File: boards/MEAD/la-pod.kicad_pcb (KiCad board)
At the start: 4 copper layers, 75 x 97.5 mm, 199 parts, among them J1 CONN_SFF8087, J2 PINHEADER_1x5, J3 LSHM-120-02.5-L-DV-A-N-K-TR, J4 AMG240160P-G-W6WFDW, J5 PINHEADER_1x2, U1 LMH7322, U14 TPS62173, U15 LM27761, U2 LMH7322, U3 LMH7322, U4 LMH7322, U5 STM32F031-QFN28, U6 DAC60508ZRTET, U7 TPS62170, U8 LP5907SNX-3.3/NOPB, U9 TPS62170

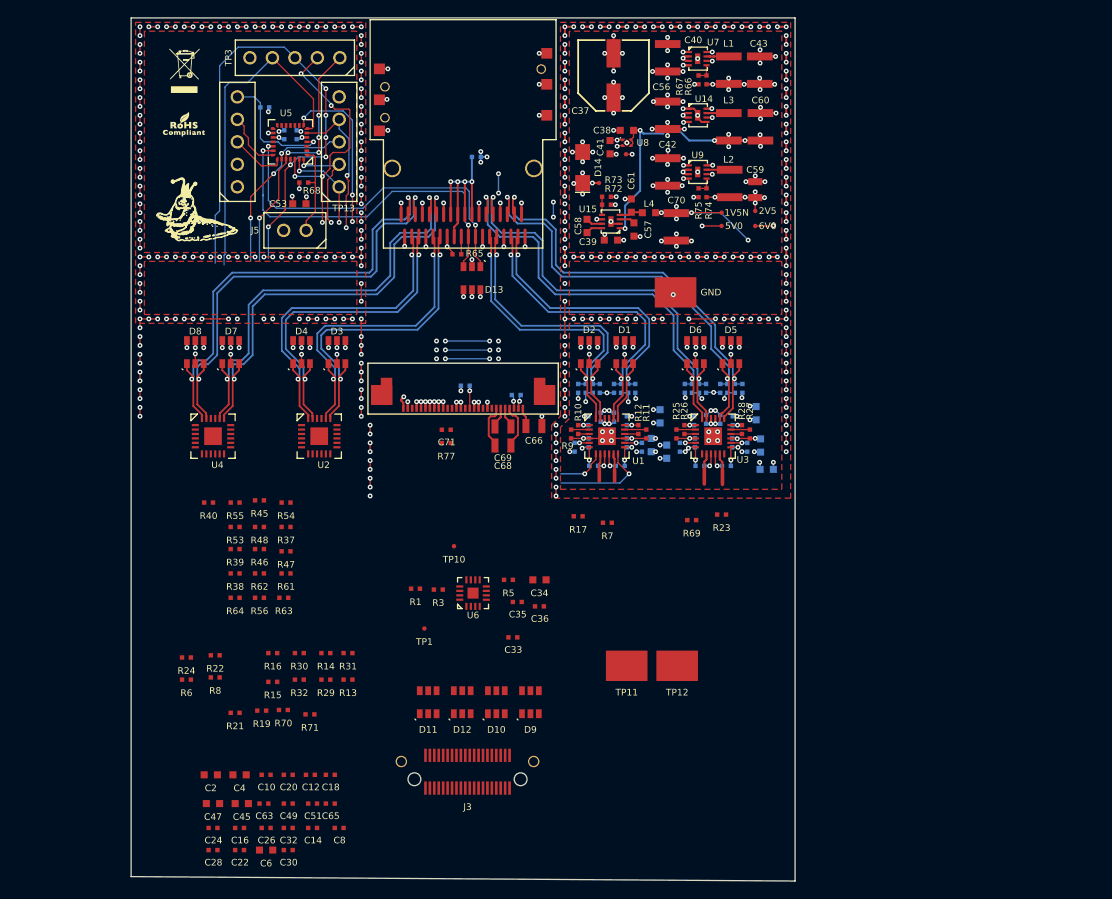
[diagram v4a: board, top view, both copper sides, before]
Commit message: Almost done laying out left side comparators
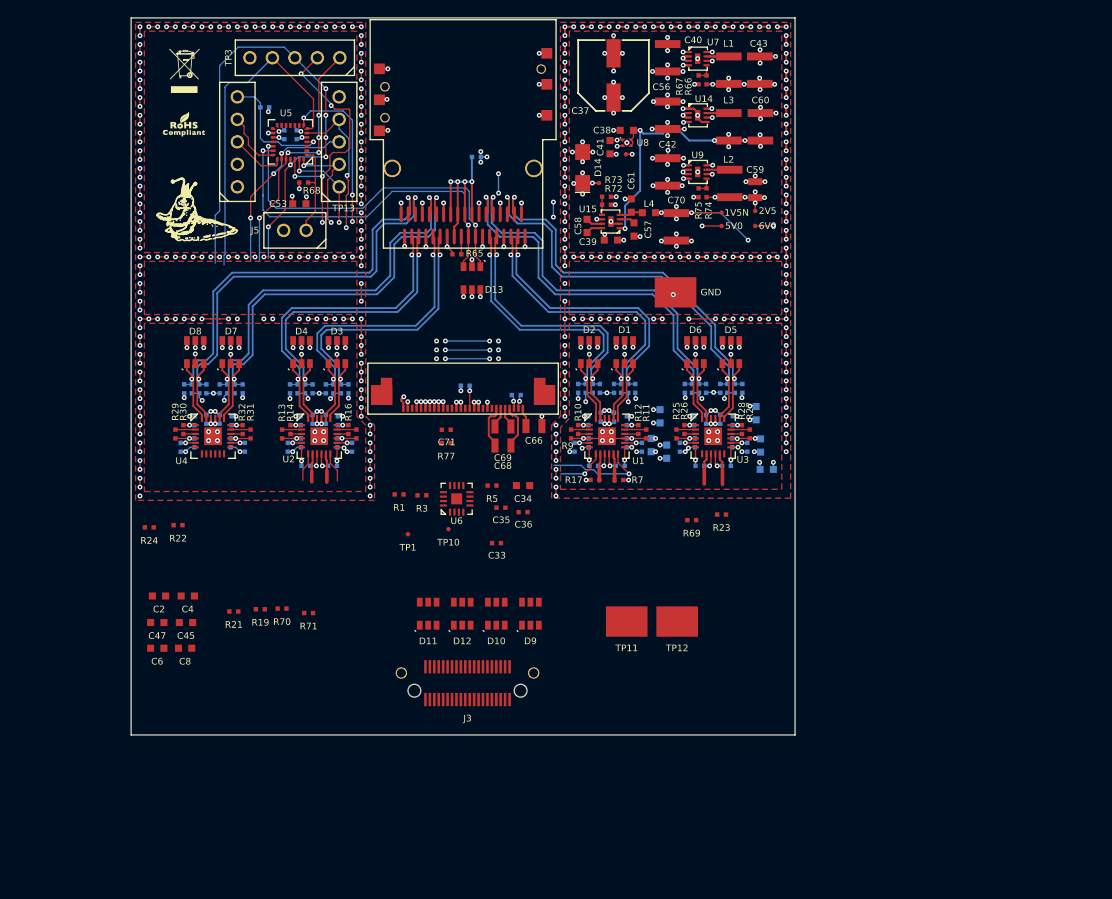
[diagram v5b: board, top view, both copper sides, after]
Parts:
- C10, C12, C14, C16, C18, C20, C22, C24, C26, C28, C30, C32, C49, C51, C63, C65, R37, R38, R39, R40, R45, R46, R47, R48, R53, R54, R55, R56, R6, R61, R62, R63, R64, R8: moved to B.Cu
- C8: footprint azonenberg_pcb:EIA_0402_CAP_NOSILK -> azonenberg_pcb:EIA_0603_CAP_NOSILK
- moved C22 49.6 mm to (50.0, 64.3), turned to 90 degrees
- moved C28 48.7 mm to (38.0, 64.3), turned to 90 degrees
- moved C30 48.5 mm to (47.1, 64.5), turned to 90 degrees
- moved C32 47.1 mm to (36.5, 64.3), turned to 90 degrees
- moved C26 46.7 mm to (51.4, 64.5), turned to 90 degrees
- moved C14 46.2 mm to (48.5, 64.3), turned to 90 degrees
- moved C24 46.0 mm to (35.1, 64.5), turned to 90 degrees
- moved C16 46.0 mm to (39.4, 64.5), turned to 90 degrees
- moved C49 42.1 mm to (35.1, 67.0), turned to 270 degrees
- moved C51 41.8 mm to (39.2, 67.0), turned to 270 degrees
- moved C63 41.0 mm to (47.2, 67.0), turned to 270 degrees
- moved C65 40.8 mm to (51.3, 67.0), turned to 270 degrees
- moved C10 38.2 mm to (33.6, 67.5), turned to 270 degrees
- moved C20 37.3 mm to (40.9, 67.5), turned to 270 degrees
- moved C12 37.1 mm to (45.7, 67.5), turned to 270 degrees
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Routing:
- net /GND: track 873.3 -> 962.7 mm, vias 455 -> 483
- net /1V5_N: track 94.2 -> 157.7 mm, vias 20 -> 32
- net /2V5: track 215.2 -> 274.6 mm, vias 58 -> 72
- net /6V0: track 98.6 -> 150.4 mm, vias 15 -> 19
- net /Comparators/VREF2: track 0.00 -> 3.38 mm
- net /Comparators/VREF3: track 0.00 -> 3.25 mm
- net /Comparators/CH2: track 0.00 -> 3.23 mm
- net /Comparators/CH3: track 0.00 -> 3.19 mm
- net Net-(R31-Pad2): track 0.00 -> 2.25 mm
- net Net-(R29-Pad2): track 0.00 -> 2.25 mm
- net Net-(R15-Pad2): track 0.00 -> 2.20 mm
- net Net-(R13-Pad2): track 0.00 -> 2.20 mm
- net Net-(R8-Pad2): track 0.00 -> 2.10 mm, vias 0 -> 1
- net Net-(R6-Pad2): track 0.00 -> 2.10 mm, vias 0 -> 1
- net Net-(R6-Pad1): track 0.00 -> 2.06 mm, vias 0 -> 1
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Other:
- board size 75 x 97.5 mm -> 75 x 81 mm

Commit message: Continued layout on MEAD. All comparators done, LVDS length matched, DAC routed
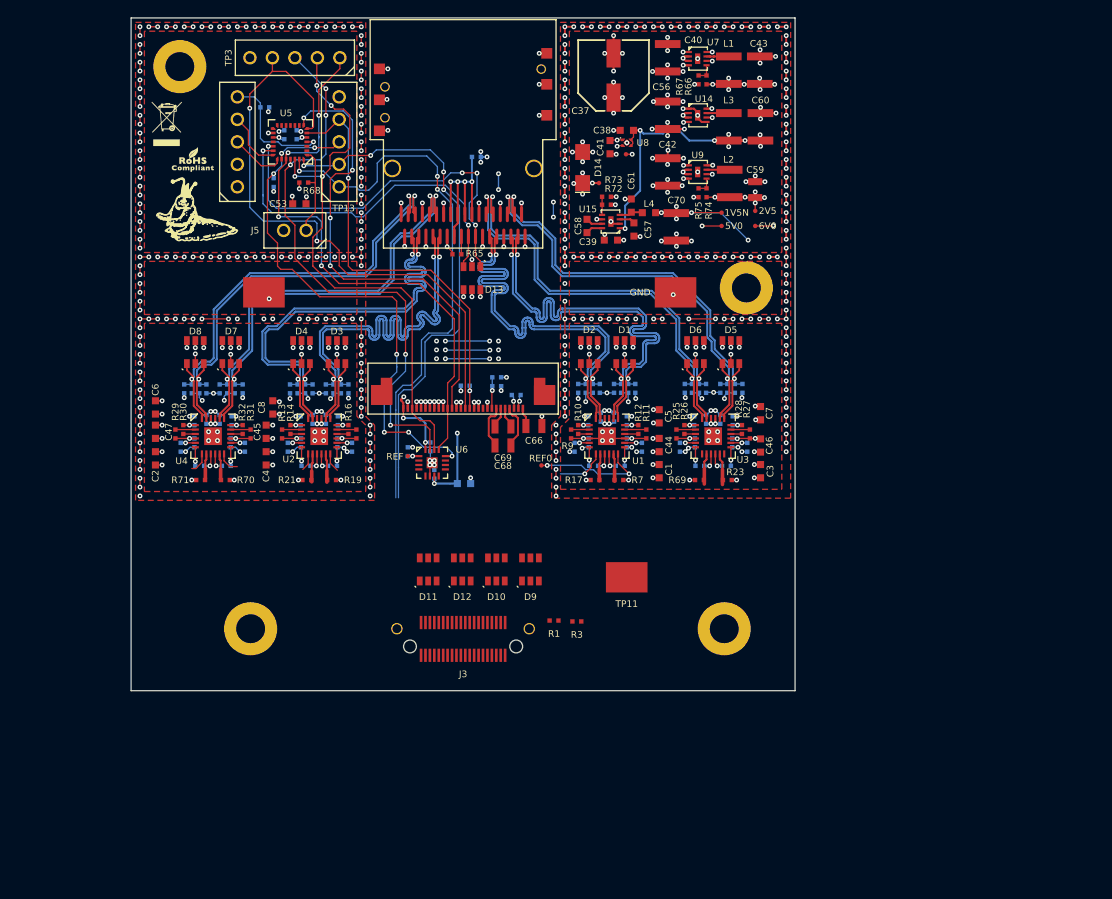
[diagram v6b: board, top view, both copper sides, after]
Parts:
- added MH1: SCREWHOLE_4_40, azonenberg_pcb:MECHANICAL_CLEARANCEHOLE_4_40, F.Cu at (33.5, 24.5)
- added MH2: SCREWHOLE_4_40, azonenberg_pcb:MECHANICAL_CLEARANCEHOLE_4_40, F.Cu at (97.5, 49.5)
- added MH3: SCREWHOLE_4_40, azonenberg_pcb:MECHANICAL_CLEARANCEHOLE_4_40, F.Cu at (41.5, 88.0)
- added MH4: SCREWHOLE_4_40, azonenberg_pcb:MECHANICAL_CLEARANCEHOLE_4_40, F.Cu at (95.0, 88.0)
- C1, C3, C44, C46, C5, C7: moved to F.Cu
- C33, C34, C35, C36, C71, R22, R24, R5, R77: moved to B.Cu
- moved TP12 59.7 mm to (43.0, 50.0)
- moved R5 42.2 mm to (44.1, 37.6), turned to 270 degrees
- moved C8 28.9 mm to (44.0, 63.0), turned to 90 degrees
- moved C6 27.2 mm to (30.8, 63.0), turned to 90 degrees
- moved C45 23.4 mm to (43.2, 65.8), turned to 90 degrees
- moved R1 22.6 mm to (75.8, 87.1)
- moved R3 22.6 mm to (78.3, 87.2)
- moved C47 21.6 mm to (30.8, 65.8), turned to 90 degrees
- moved R71 19.4 mm to (35.9, 71.2)
- moved C4 17.9 mm to (43.2, 68.8), turned to 90 degrees
- moved R21 17.0 mm to (47.9, 71.2)
- moved R19 16.7 mm to (50.6, 71.2), turned to 180 degrees
- moved R70 15.9 mm to (38.6, 71.2), turned to 180 degrees
- moved C2 15.6 mm to (30.8, 68.8), turned to 90 degrees
- moved C36 14.7 mm to (59.2, 68.0), turned to 90 degrees
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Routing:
- net /GND: track 962.7 -> 1047.7 mm, vias 483 -> 501
- net /PROBE_I2C_SCL: track 10.6 -> 63.7 mm, vias 2 -> 3
- net /PROBE_I2C_SDA: track 12.1 -> 61.3 mm, vias 2 -> 4
- net /DAC/DAC_CS_N: track 21.2 -> 62.4 mm, vias 3 -> 7
- net /DAC/DAC_SCK: track 28.8 -> 65.9 mm, vias 5 -> 4
- net /DAC/DAC_MOSI: track 29.8 -> 64.8 mm, vias 5 -> 4
- net /MCU/LCD_RST_N: track 18.6 -> 53.2 mm, vias 3 -> 4
- net /MCU/LCD_CTRL_DATA: track 37.4 -> 70.2 mm, vias 0 -> 2
- net /MCU/LCD_CS_N: track 19.8 -> 48.8 mm, vias 3 -> 2
- net /2V5: track 274.6 -> 293.9 mm, vias 72 -> 74
- net /5V0: track 114.5 -> 133.5 mm, vias 14 -> 16
- net /3V3: track 116.4 -> 131.9 mm, vias 12 -> 16
- net /TX1_N: track 36.1 -> 50.2 mm
- net /TX1_P: track 36.1 -> 50.2 mm
- net /TX2_N: track 37.3 -> 50.3 mm
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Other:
- board size 75 x 81 mm -> 75 x 76 mm
- board text added: "REF"
- board text added: "REF0"

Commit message: Updating file: la-pod.kicad_pcb with current fully routed design
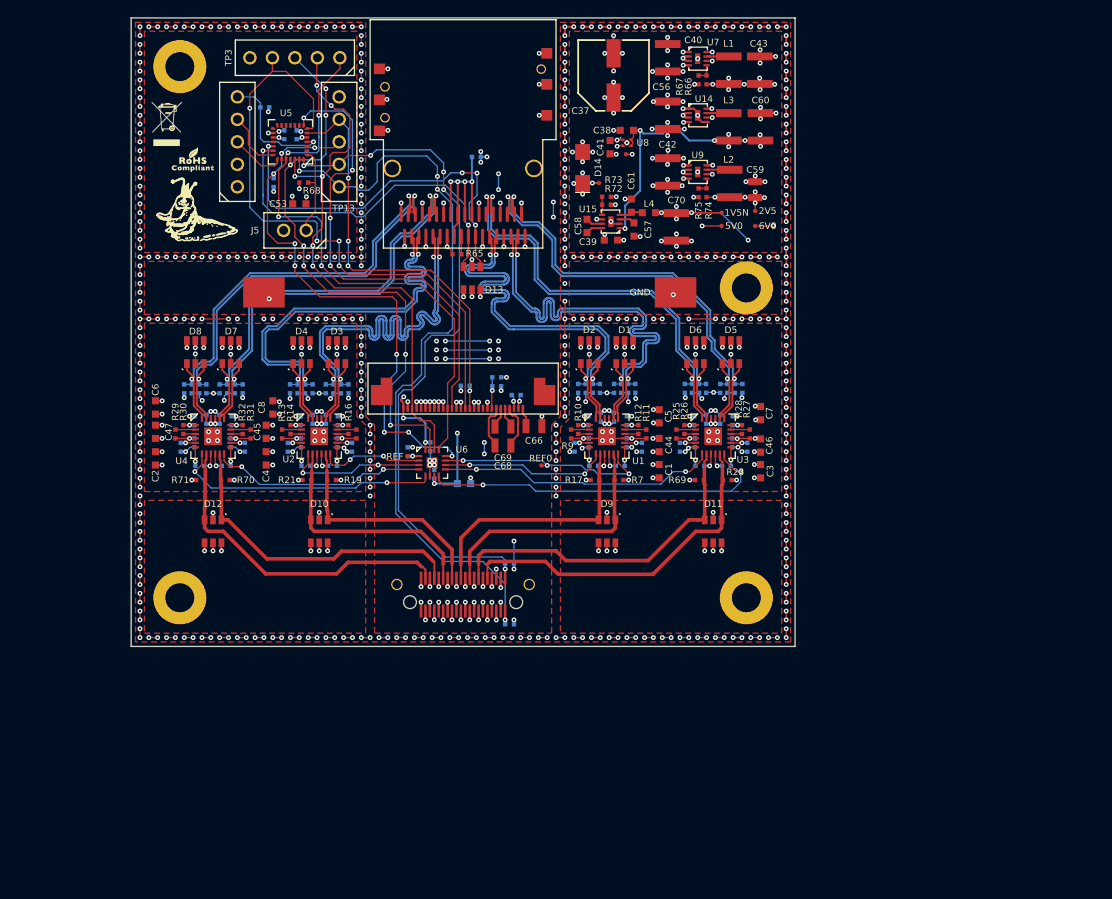
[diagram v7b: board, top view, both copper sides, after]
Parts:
- removed TP11: TESTCLIP, azonenberg_pcb:TESTPOINT_SMT_KEYSTONE_5016
- R1, R3: moved to B.Cu
- moved D11 32.5 mm to (93.8, 77.0), turned to 180 degrees
- moved D12 28.5 mm to (37.2, 77.0), turned to 180 degrees
- moved D10 20.5 mm to (49.2, 77.0), turned to 180 degrees
- moved D9 9.66 mm to (81.8, 77.0), turned to 180 degrees
- moved MH3 8.73 mm to (33.5, 84.5)
- moved R1 8.16 mm to (70.8, 80.7), turned to 180 degrees
- moved R3 7.61 mm to (70.8, 87.5), turned to 180 degrees
- moved J3 5.00 mm to (65.5, 85.0)
- moved MH4 4.30 mm to (97.5, 84.5)
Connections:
- J3 pad 11: /Comparators/CH2 -> /Comparators/CH3
- J3 pad 15: /Comparators/CH3 -> /Comparators/CH2
- J3 pad 19: /Comparators/CH4 -> /Comparators/CH1
- J3 pad 23: /Comparators/CH5 -> /Comparators/CH0
- J3 pad 27: /Comparators/CH6 -> /Comparators/CH5
- J3 pad 3: /Comparators/CH0 -> /Comparators/CH7
- J3 pad 31: /Comparators/CH7 -> /Comparators/CH4
- J3 pad 7: /Comparators/CH1 -> /Comparators/CH6
- U6 pad 10: /Comparators/VREF6 -> /Comparators/VREF1
- U6 pad 11: /Comparators/VREF7 -> /VREF0
- U6 pad 2: /VREF0 -> /Comparators/VREF2
- U6 pad 3: /Comparators/VREF1 -> /Comparators/VREF3
- U6 pad 4: /Comparators/VREF2 -> /Comparators/VREF6
- U6 pad 5: /Comparators/VREF3 -> /Comparators/VREF7
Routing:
- net /GND: track 1047.7 -> 1302.8 mm, vias 501 -> 643
- net /5V0: track 133.5 -> 210.3 mm, vias 16 -> 28
- net /Comparators/VREF4: track 0.00 -> 39.8 mm, vias 0 -> 2
- net /Comparators/CH4: track 3.57 -> 39.5 mm
- net /Comparators/CH5: track 3.50 -> 38.3 mm
- net /Comparators/CH7: track 2.81 -> 37.2 mm
- net /Comparators/CH6: track 2.93 -> 36.0 mm
- net /3V3: track 131.9 -> 163.7 mm, vias 16 -> 22
- net /Comparators/VREF5: track 0.00 -> 31.5 mm, vias 0 -> 2
- net /Comparators/VREF7: track 2.39 -> 30.0 mm, vias 0 -> 2
- net /Comparators/CH0: track 3.13 -> 29.2 mm
- net /Comparators/CH1: track 3.08 -> 28.6 mm
- net /Comparators/CH3: track 3.19 -> 27.5 mm
- net /PROBE_I2C_SCL: track 63.7 -> 86.7 mm, vias 3 -> 4
- net /Comparators/CH2: track 3.23 -> 26.2 mm
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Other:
- board size 75 x 76 mm -> 75 x 71 mm

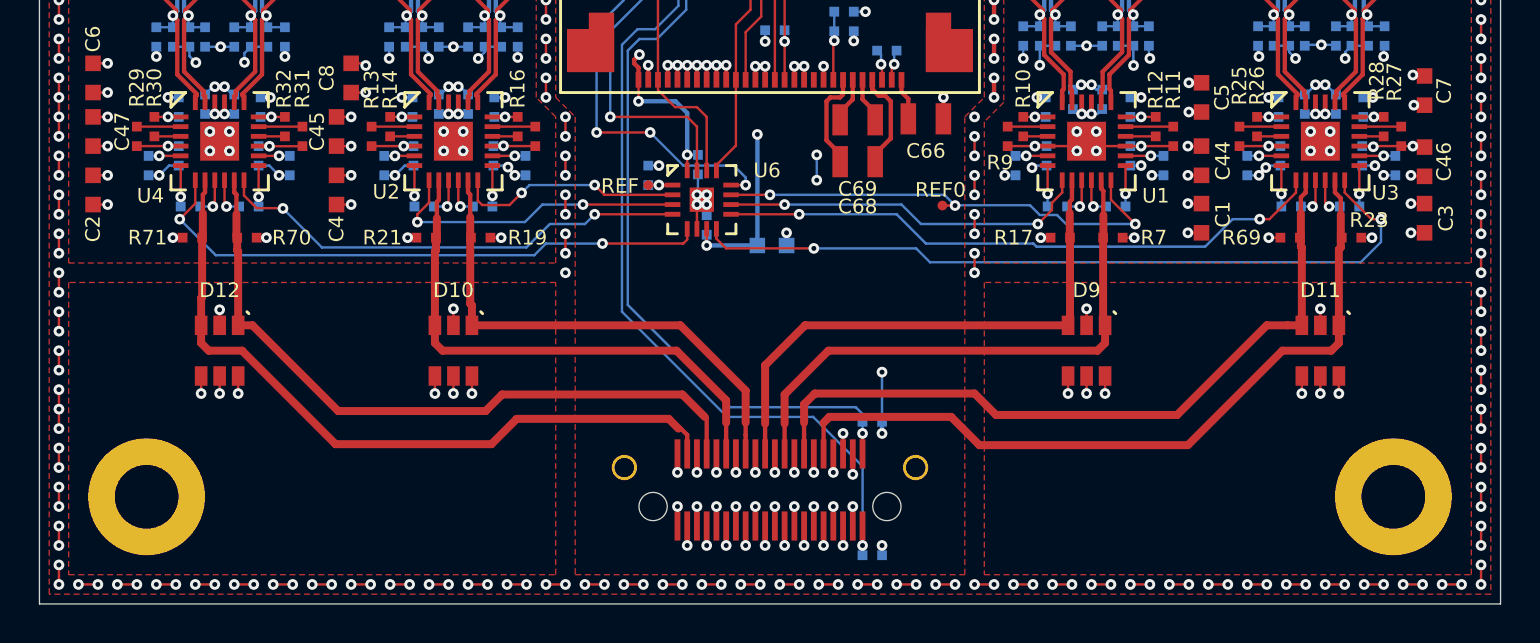
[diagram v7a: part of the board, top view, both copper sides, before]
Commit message: Length matched input signals, tweaks to top layer shield routing
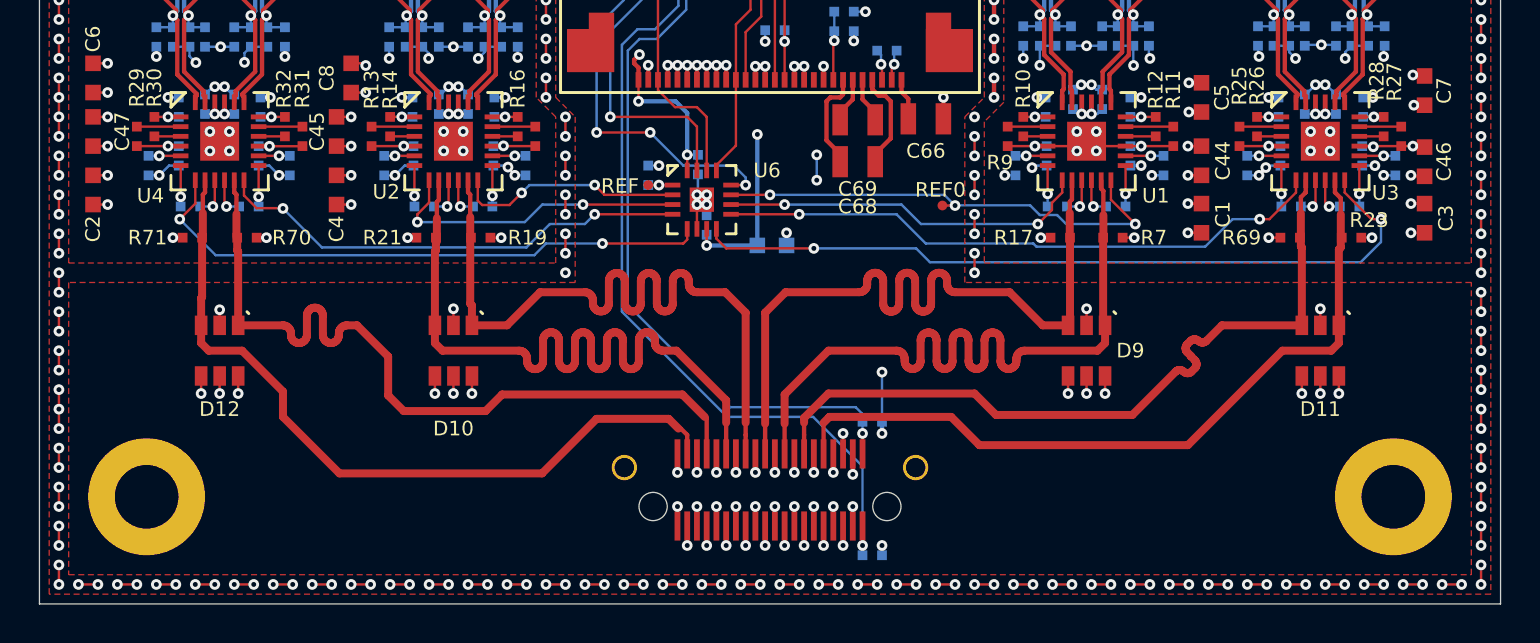
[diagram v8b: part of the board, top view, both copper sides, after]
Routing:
- net /Comparators/CH2: track 26.2 -> 39.3 mm
- net /Comparators/CH3: track 27.5 -> 39.5 mm
- net /Comparators/CH1: track 28.6 -> 39.4 mm
- net /Comparators/CH0: track 29.2 -> 39.5 mm
- net /Comparators/CH6: track 36.0 -> 41.2 mm
- net /Comparators/CH7: track 37.2 -> 39.2 mm
- net /Comparators/CH5: track 38.3 -> 39.4 mm
